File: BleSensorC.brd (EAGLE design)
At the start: 29 x 40.5 mm, 20 parts, among them IC1 PIC16LF18446-I_SS, IC2 SI7020-A20-GM, Q1 SI2333DDS-T1-GE3, T1 VEMT2523SLX01, U1 RN4871-I

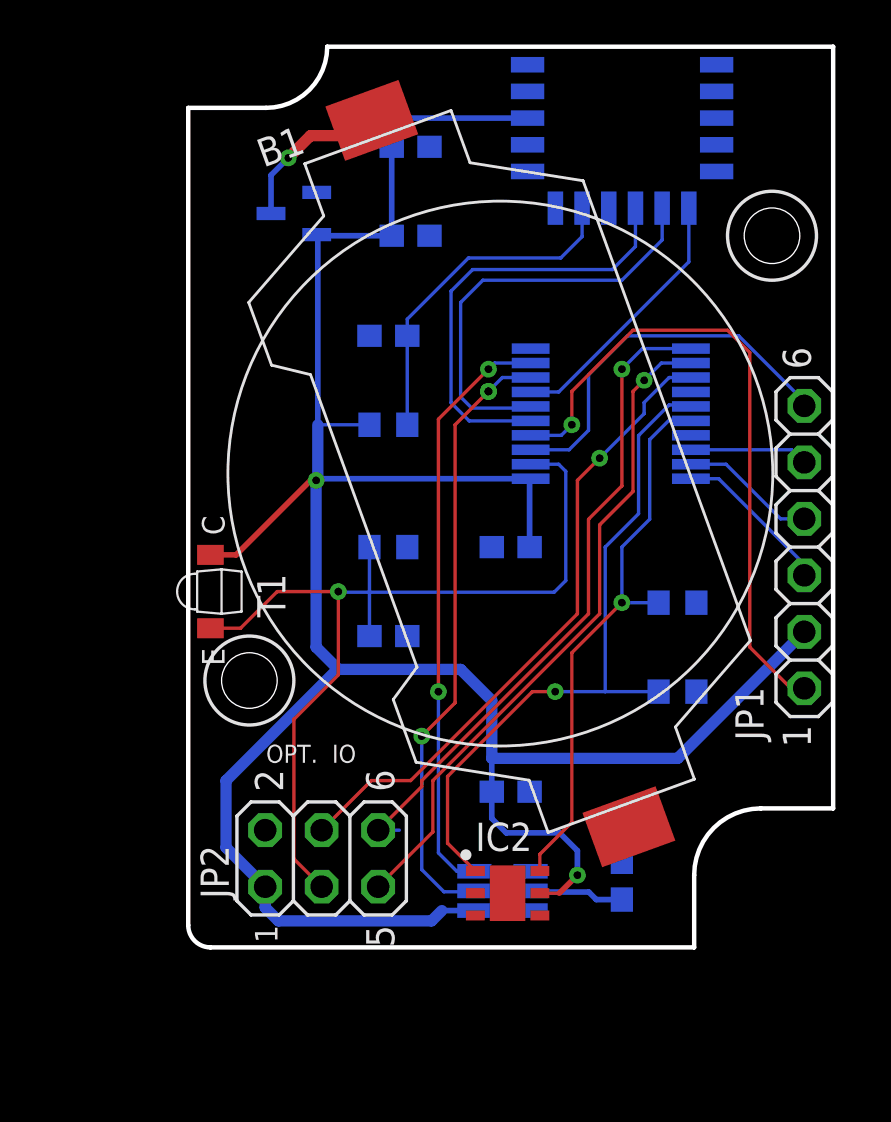
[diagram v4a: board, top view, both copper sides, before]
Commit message: IC1 to bottom side
IC1 to bottom side
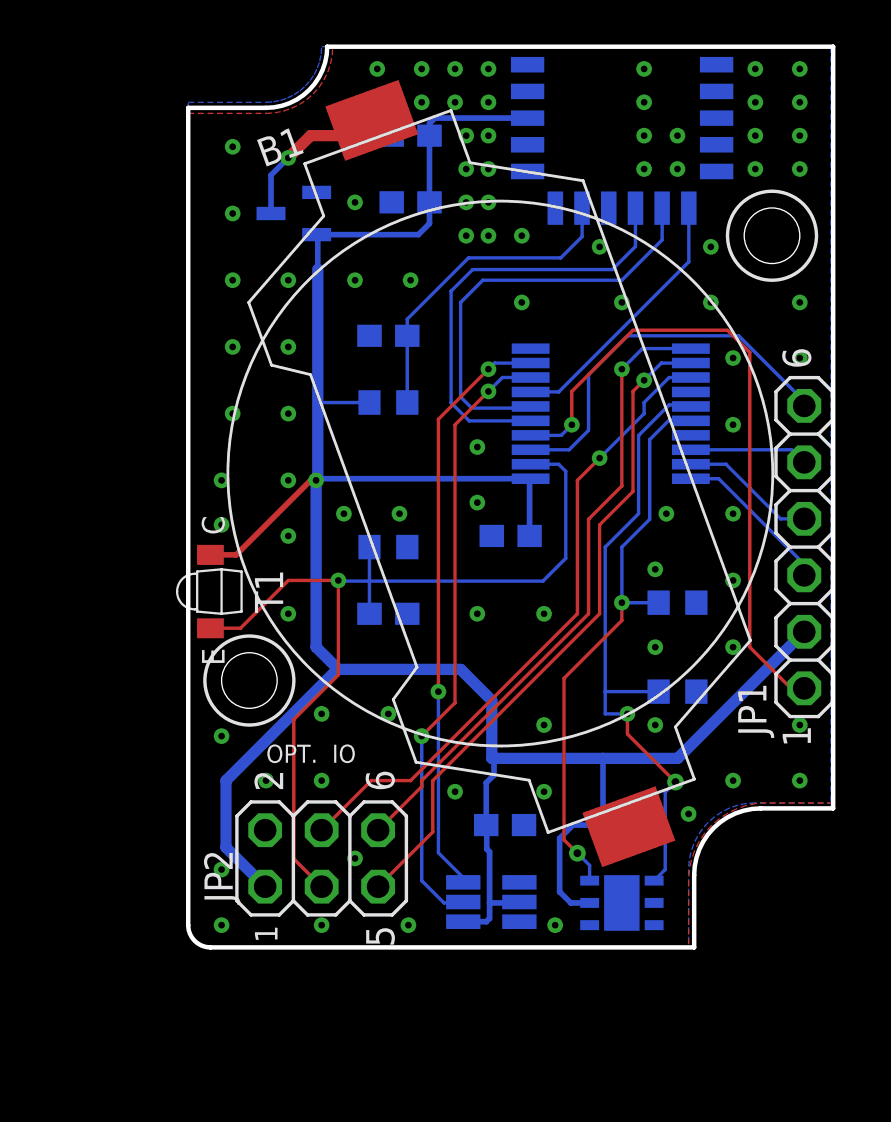
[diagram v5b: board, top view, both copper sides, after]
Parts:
- moved C6 5.81 mm to (14.2, 5.50), turned to 180 degrees
- moved C5 5.22 mm to (19.5, 5.50)
- moved IC2 5.16 mm to (19.5, 2.00), flipped to the bottom
- moved C2 1.50 mm to (10.0, 33.5), turned to 0 degrees
- moved C1 1.00 mm to (9.00, 15.0)
- moved R4 1.00 mm to (9.00, 24.5)
- moved MK1 0.71 mm to (13.6, 2.04)
- moved C3 0.50 mm to (10.0, 36.5), turned to 0 degrees
- moved C4 0.50 mm to (14.5, 18.5)
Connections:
- removed net RB7: IC1.10
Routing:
- net SDA1: track 30.9 -> 28.3 mm, vias 1 -> 2
- net VDD: track 123.0 -> 120.3 mm, vias 2 -> 1
- net RST: track 15.8 -> 14.5 mm
- net IMP: track 42.1 -> 41.1 mm
- net RB6: track 29.7 -> 28.8 mm
- net SCL1: track 25.3 -> 25.8 mm, vias 1 -> 2
- net SCL2: vias 3 -> 2
- net GND: vias 0 -> 86
- added copper zone on layer 1, net GND
- added copper zone on layer 16, net GND
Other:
- board text added: "BLE-SENSOR-C v1.00"
- board text removed: "BLE SENSOR C v1.00"

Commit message: U1 placing
U1 placing
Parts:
- moved IC2 0.50 mm to (19.0, 2.00)
- moved U1 0.25 mm to (20.0, 37.2)
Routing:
- net SDA1: track 28.3 -> 28.8 mm

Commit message: Fixed layout, BOM & Gerber files
Fixed layout, BOM & Gerber files
ITEAD PCBA Enquiry
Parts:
- added T2: VEMT2523SLX01, esao:VEMT2523SL
- moved U1 0.25 mm to (20.0, 37.0)
- moved T1 0.10 mm to (1.10, 16.0)
- turned MK1 to 0 degrees
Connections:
- new net RA2: IC1.17, U1.16
- net IMP: now also T2.E
- net VDD: now also T2.C
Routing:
- net RA2: track 0.00 -> 33.1 mm, vias 0 -> 2
- net IMP: track 41.1 -> 51.2 mm
- net VDD: track 119.9 -> 128.0 mm
- net SDA2: track 26.5 -> 32.9 mm
- net SCL2: track 27.7 -> 32.0 mm, vias 2 -> 4
- net GND: vias 86 -> 84
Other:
- board size 29 x 40.5 mm -> 29 x 40.2 mm
- board text added: "OPTIONAL IO"
- board text removed: "OPT. IO"

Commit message: Seeed order v1.00
Footprint R0805 and C0805
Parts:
- C1, C2, C3, C4, C5, C6, C7: device resistor:C0603 -> resistor:C0805
- R1, R2, R3, R4: device resistor:R0603 -> resistor:R0805
- moved C3 0.71 mm to (9.50, 37.0)
- moved C1 0.50 mm to (9.00, 14.5)
- moved C2 0.50 mm to (9.50, 33.5)
- moved R4 0.50 mm to (9.00, 24.0)
- moved C6 0.25 mm to (14.5, 5.50)
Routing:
- net VDD: track 128.0 -> 129.4 mm
- net RST: track 14.1 -> 14.7 mm
